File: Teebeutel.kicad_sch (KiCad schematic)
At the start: 177 parts, among them J1 USB_A, J10 Conn_01x30_Female, J11 Battery, J2 Conn_01x06_Female, J3 Conn_01x06_Female, J4 USB_C_Receptacle_USB2.0, J5 RJ45_Shielded, J6 Conn_01x10_Female, J7 Conn_01x10_Female, J8 Micro_SD_Card, J9 RJ45_Shielded, M1 Motor_DC, Q1 AO3400, Q2 AO3400, Q3 S8050, Q4 AO3400, Q5 AO3400, Q6 S8050, Q7 AO3400, Q8 AO3400, Q9 AO3400, SW1 K1-1506SN-01, SW2 SW_SPST, U1 CH340C, U10 LIS2DE12, U11 TLV70018_SOT23-5, U12 TLV62569DBVR, U13 MCP73831-2-OT, U2 SDB628, U3 RM-V8xxC_TR1, U4 PCA9539BS,118, U5 TXB0104RUT, U6 ESP32-WROOM-32E(16MB), U7 SRV05-4, U8 SGP30, U9 PPSI262

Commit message: small changes
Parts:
- C?: renamed from C27; JLC 0603 -> (none)
- C?: renamed from C28; JLC 0603 -> (none)
- C?: renamed from C40; JLC 0603 -> (none)
- C?: renamed from C47; JLC 0603 -> (none)
- C?: renamed from C10; JLC 0603 -> (none)
- C?: renamed from C11; JLC 0603 -> (none)
- C?: renamed from C17; JLC 0603 -> (none)
- C?: renamed from C26; JLC 0603 -> (none)
- C?: renamed from C25; JLC 0603 -> (none)
- C?: renamed from C16; JLC 0603 -> (none)
- C?: renamed from C21; JLC 0603 -> (none)
- C?: renamed from C22; JLC 0603 -> (none)
- C?: renamed from C20; JLC 0603 -> (none)
- C?: renamed from C8; JLC 0603 -> (none)
- C?: renamed from C9; JLC 0603 -> (none)
- C?: renamed from C45; JLC 0603 -> (none)
- C?: renamed from C34; JLC 0603 -> (none)
- C?: renamed from C33; JLC 0603 -> (none)
- C?: renamed from C46; JLC 0603 -> (none)
- C?: renamed from C7; JLC 0603 -> (none)
- C?: renamed from C6; JLC 0603 -> (none)
- C?: renamed from C4; JLC 0603 -> (none)
- C?: renamed from C5; JLC 0603 -> (none)
- C?: renamed from C43; JLC 0603 -> (none)
- C?: renamed from C42; JLC 0603 -> (none)
- C?: renamed from C41; JLC 0603 -> (none)
- C?: renamed from C44; JLC 0603 -> (none)
- C?: renamed from C36; JLC 0603 -> (none)
- C?: renamed from C35; JLC 0603 -> (none)
- C?: renamed from C38; JLC 0603 -> (none)
- C?: renamed from C37; JLC 0603 -> (none)
- C?: renamed from C15; JLC 0603 -> (none)
- C?: renamed from C14; JLC 0603 -> (none)
- C?: renamed from C13; JLC 0603 -> (none)
- C?: renamed from C12; JLC 0603 -> (none)
- C?: renamed from C29; JLC 0603 -> (none)
- C?: renamed from C30; JLC 0603 -> (none)
- C?: renamed from C31; JLC 0603 -> (none)
- C?: renamed from C32; JLC 0603 -> (none)
- C?: renamed from C48; JLC 0603 -> (none)
- C?: renamed from C18; JLC 0603 -> (none)
- C?: renamed from C19; JLC 0603 -> (none)
- C?: renamed from C24; JLC 0603 -> (none)
- C?: renamed from C23; JLC 0603 -> (none)
- C?: renamed from C1; JLC 0603 -> (none)
- C?: renamed from C3; JLC 0603 -> (none)
- C?: renamed from C2; JLC 0603 -> (none)
- C?: renamed from C39; JLC 0603 -> (none)
- D1: renamed from D7; JLC 4.0x2.0mm -> (none)
- D10: renamed from D16; JLC 4.0x2.0mm -> (none)
- D11: renamed from D17; JLC 4.0x2.0mm -> (none)
- D12: renamed from D18; JLC 4.0x2.0mm -> (none)
- D2: renamed from D8; JLC 4.0x2.0mm -> (none)
- D3: renamed from D9; JLC 4.0x2.0mm -> (none)
- D4: renamed from D10; JLC 4.0x2.0mm -> (none)
- D5: renamed from D11; JLC 4.0x2.0mm -> (none)
- D6: renamed from D12; JLC 4.0x2.0mm -> (none)
- D7: renamed from D13; JLC 4.0x2.0mm -> (none)
- D8: renamed from D14; JLC 4.0x2.0mm -> (none)
- D9: renamed from D15; JLC 4.0x2.0mm -> (none)
- D?: renamed from D3; JLC SOD-523 -> (none)
- D?: renamed from D5; JLC SOD-523 -> (none)
- D?: renamed from D4; JLC DO-214AC -> (none)
- D?: renamed from D19; JLC LED_0805 -> (none)
- D?: renamed from D20; JLC LED_0805 -> (none)
- D?: renamed from D1; JLC DO-214AC -> (none)
- D?: renamed from D2; JLC LED-SMD -> (none)
- D?: renamed from D6; JLC SOD-523 -> (none)
- F?: renamed from F1; JLC SMD0805 -> (none)
- F?: renamed from F2; JLC SMD0805 -> (none)
- J?: renamed from J9; JLC RJ45-TH -> (none)
- J?: renamed from J8; JLC 14.5x14.75x1.85mm -> (none)
- J?: renamed from J10; JLC 30P -> (none)
- J?: renamed from J1; now left out of the parts list
- J?: renamed from J5; JLC RJ45-TH -> (none)
- L?: renamed from L1; JLC 1210 -> (none)
- Q?: renamed from Q6; JLC SOT-23-3 -> (none)
- Q?: renamed from Q3; JLC SOT-23-3 -> (none)
- R?: renamed from R3; JLC 0603 -> (none)
- R?: renamed from R8; JLC 0603 -> (none)
- R?: renamed from R27; JLC 0603 -> (none)
- R?: renamed from R36; JLC R0603 -> (none)
- R?: renamed from R11; JLC 0603 -> (none)
- R?: renamed from R14; JLC 0603 -> (none)
- R?: renamed from R38; JLC R0603 -> (none)
- R?: renamed from R39; JLC R0603 -> (none)
- R?: renamed from R9; JLC 0603 -> (none)
- R?: renamed from R10; JLC 0603 -> (none)
- R?: renamed from R20; JLC 0603 -> (none)
- R?: renamed from R21; JLC 0603 -> (none)
- R?: renamed from R5; JLC 0603 -> (none)
- R?: renamed from R18; JLC 0603 -> (none)
- R?: renamed from R19; JLC 0603 -> (none)
- R?: renamed from R17; JLC 0603 -> (none)
- R?: renamed from R28; JLC 0603 -> (none)
- R?: renamed from R30; JLC 0603 -> (none)
- R?: renamed from R13; JLC 0603 -> (none)
- R?: renamed from R34; JLC 0603 -> (none)
- R?: renamed from R33; JLC 0603 -> (none)
- R?: renamed from R15; JLC 0603 -> (none)
- R?: renamed from R16; JLC 0603 -> (none)
- R?: renamed from R35; JLC 0603 -> (none)
- R?: renamed from R37; JLC 0603 -> (none)
- R?: renamed from R4; JLC 0603 -> (none)
- R?: renamed from R7; JLC 0603 -> (none)
- R?: renamed from R6; JLC 0603 -> (none)
- R?: renamed from R26; JLC 0603 -> (none)
- R?: renamed from R12; JLC 0603 -> (none)
- R?: renamed from R32; JLC 0603 -> (none)
- R?: renamed from R31; JLC 0603 -> (none)
- R?: renamed from R23; JLC R0603 -> (none)
- R?: renamed from R2; JLC R0603 -> (none)
- R?: renamed from R1; JLC R0603 -> (none)
- R?: renamed from R24; JLC R0603 -> (none)
- R?: renamed from R22; JLC 0603 -> (none)
- R?: renamed from R29; JLC 0603 -> (none)
- R?: renamed from R25; JLC 0603 -> (none)
- SW?: renamed from SW1; JLC KEY-SMD -> (none)
- SW?: renamed from SW2; JLC SW-SMD -> (none)
- TB?: renamed from TB1; now left out of the parts list
- TB?: renamed from TB2; now left out of the parts list
- U?: renamed from U9; JLC SENSOR-SMD -> (none)
- U?: renamed from U3; JLC OPTO-SMD -> (none)
- U?: renamed from U10; JLC LGA-12_2.0x2.0x0.5P -> (none)
- U?: renamed from U13; JLC SOT-23-5 -> (none)
- U?: renamed from U2; JLC SOT-23-6L -> (none)
- U?: renamed from U8; JLC DFN-6_EP_2.5x2.5x0.8P -> (none)
- U?: renamed from U11; JLC SOT-23-5 -> (none)
- U?: renamed from U7; JLC SOT-23-6L -> (none)
- renumbered J11 to J?, J7 to J?, J6 to J?, J2 to J?, J3 to J?, J4 to J?, L2 to L?, M1 to M?, Q5 to Q?, Q4 to Q?, Q7 to Q?, Q9 to Q?, Q1 to Q?, Q8 to Q?, Q2 to Q?, TP18 to TP?, TP16 to TP?, TP14 to TP?, TP13 to TP?, TP6 to TP?, TP24 to TP?, TP26 to TP?, TP25 to TP?, TP28 to TP?, TP21 to TP?, TP22 to TP?, TP4 to TP?, TP5 to TP?, TP8 to TP?, TP9 to TP?, TP10 to TP?, TP11 to TP?, TP12 to TP?, TP20 to TP?, TP23 to TP?, TP3 to TP?, TP2 to TP?, TP1 to TP?, TP7 to TP?, TP27 to TP?, TP15 to TP?, TP17 to TP?, TP19 to TP?, U6 to U?, U5 to U?, U4 to U?, U12 to U?, U1 to U?

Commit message: schematic: removed C24
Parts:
- removed C?: 100nF, Capacitor_SMD:C_0603_1608Metric, symbol Device:C
- gave numbers to parts that had none: 164
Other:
- moved on the sheet: C25

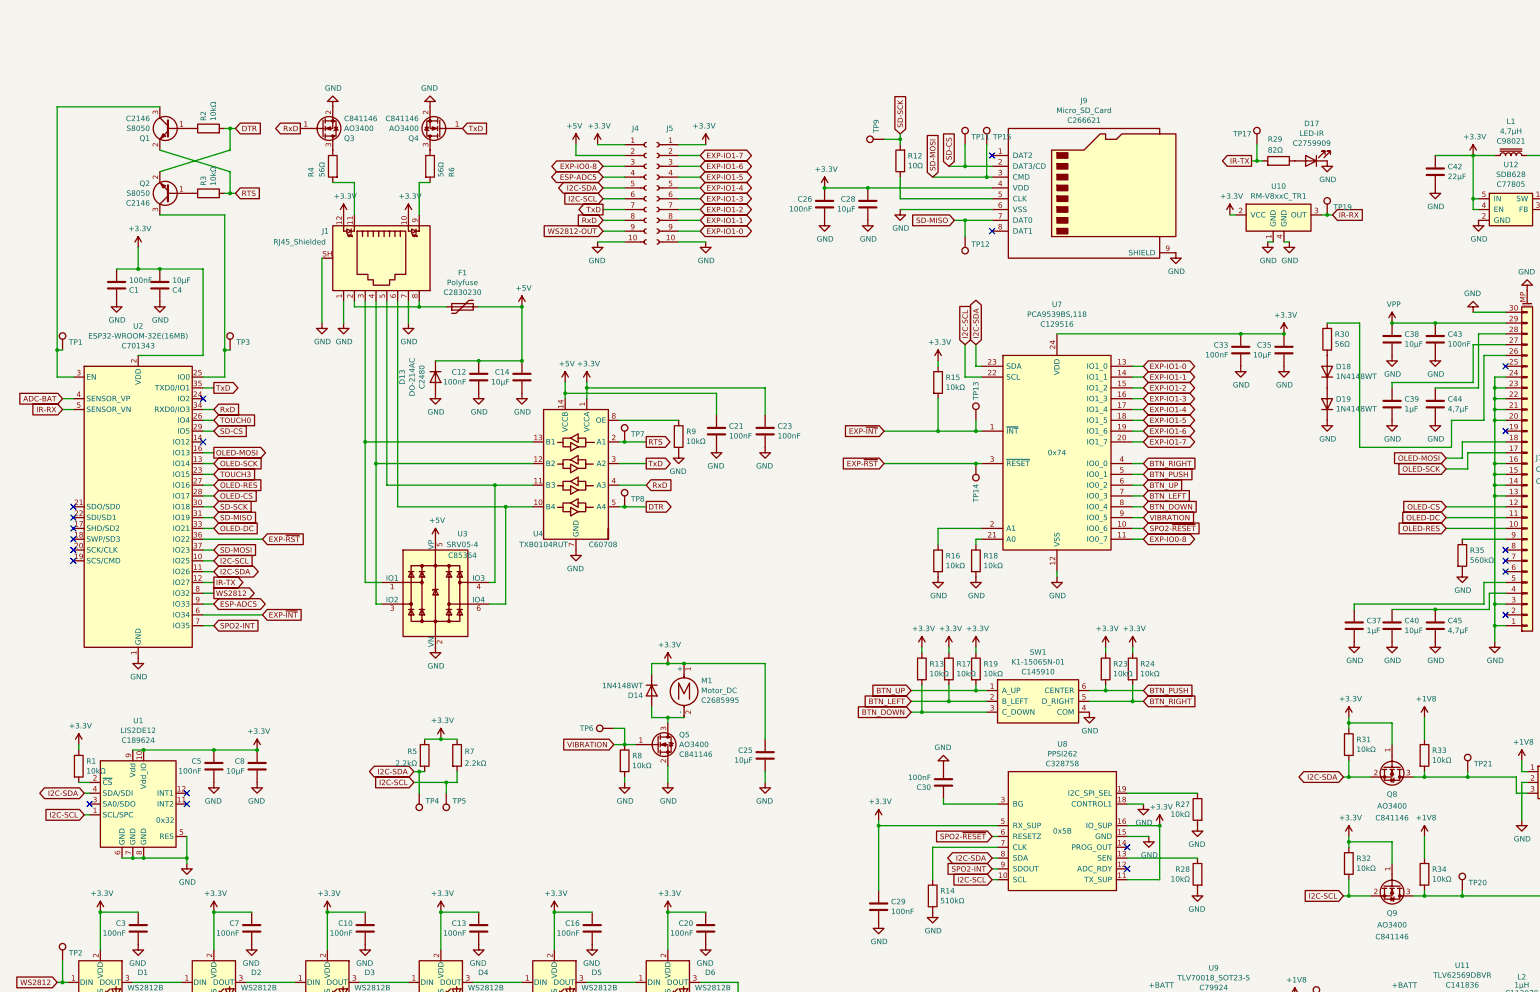
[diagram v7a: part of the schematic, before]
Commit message: schematic: removed 10k bom entry, replaced 10k with either 100k or 2.2k; fixed critical I2C level shifter error
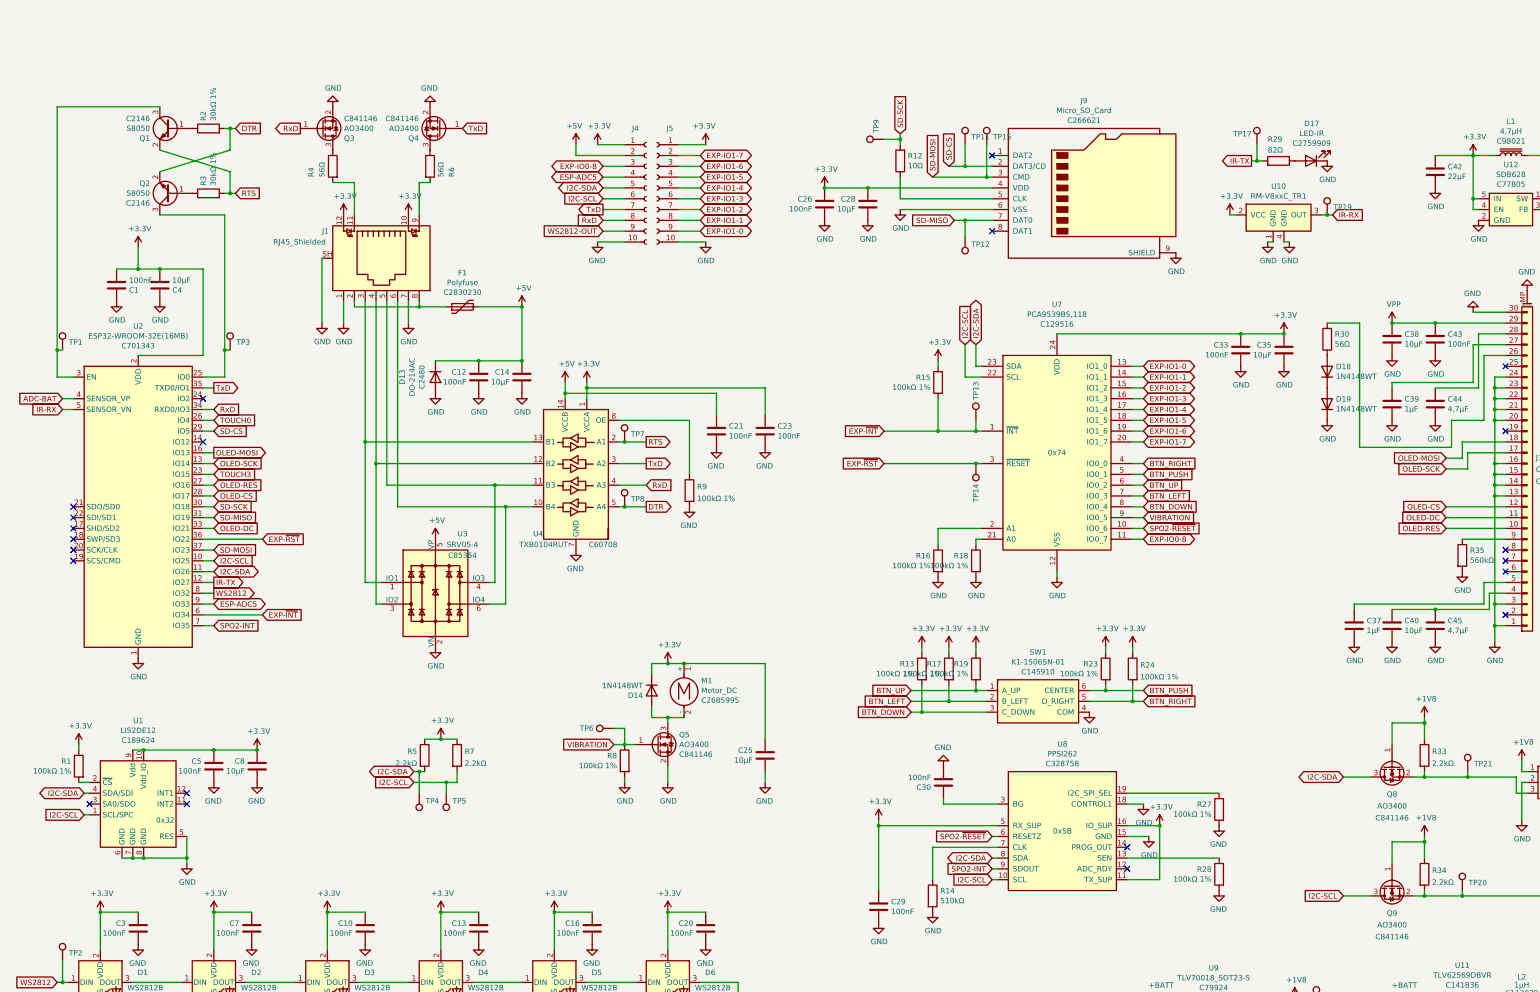
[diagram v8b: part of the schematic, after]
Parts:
- removed R31, R32: 10kΩ, Resistor_SMD:R_0603_1608Metric, symbol Device:R
- R1, R13, R15, R16, R17, R18, R19, R23, R24, R27, R28, R8, R9: value 10kΩ -> 100kΩ 1%; LCSC C25804 -> C25803
- R2, R3: value 10kΩ -> 30kΩ 1%; LCSC C25804 -> C22984
- R33, R34: value 10kΩ -> 2.2kΩ; LCSC C25804 -> C113303
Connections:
- net +1V8: now also Q8.1 (G), Q9.1 (G)
- net +3V3: no longer Q8.1 (G), Q9.1 (G)
- net I2C-SCL: now also Q9.3 (D); no longer Q9.2 (S)
- net I2C-SDA: now also Q8.3 (D); no longer Q8.2 (S)
- net at R33.2, TP21.1, U13.3 (SDA): now also Q8.2 (S); no longer Q8.3 (D)
- net at R34.2, TP20.1, U13.6 (SDC): now also Q9.2 (S); no longer Q9.3 (D)
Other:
- moved on the sheet: Q8, Q9
